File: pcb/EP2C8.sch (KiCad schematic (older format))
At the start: 1 part, among them U4 EP2C8Q208

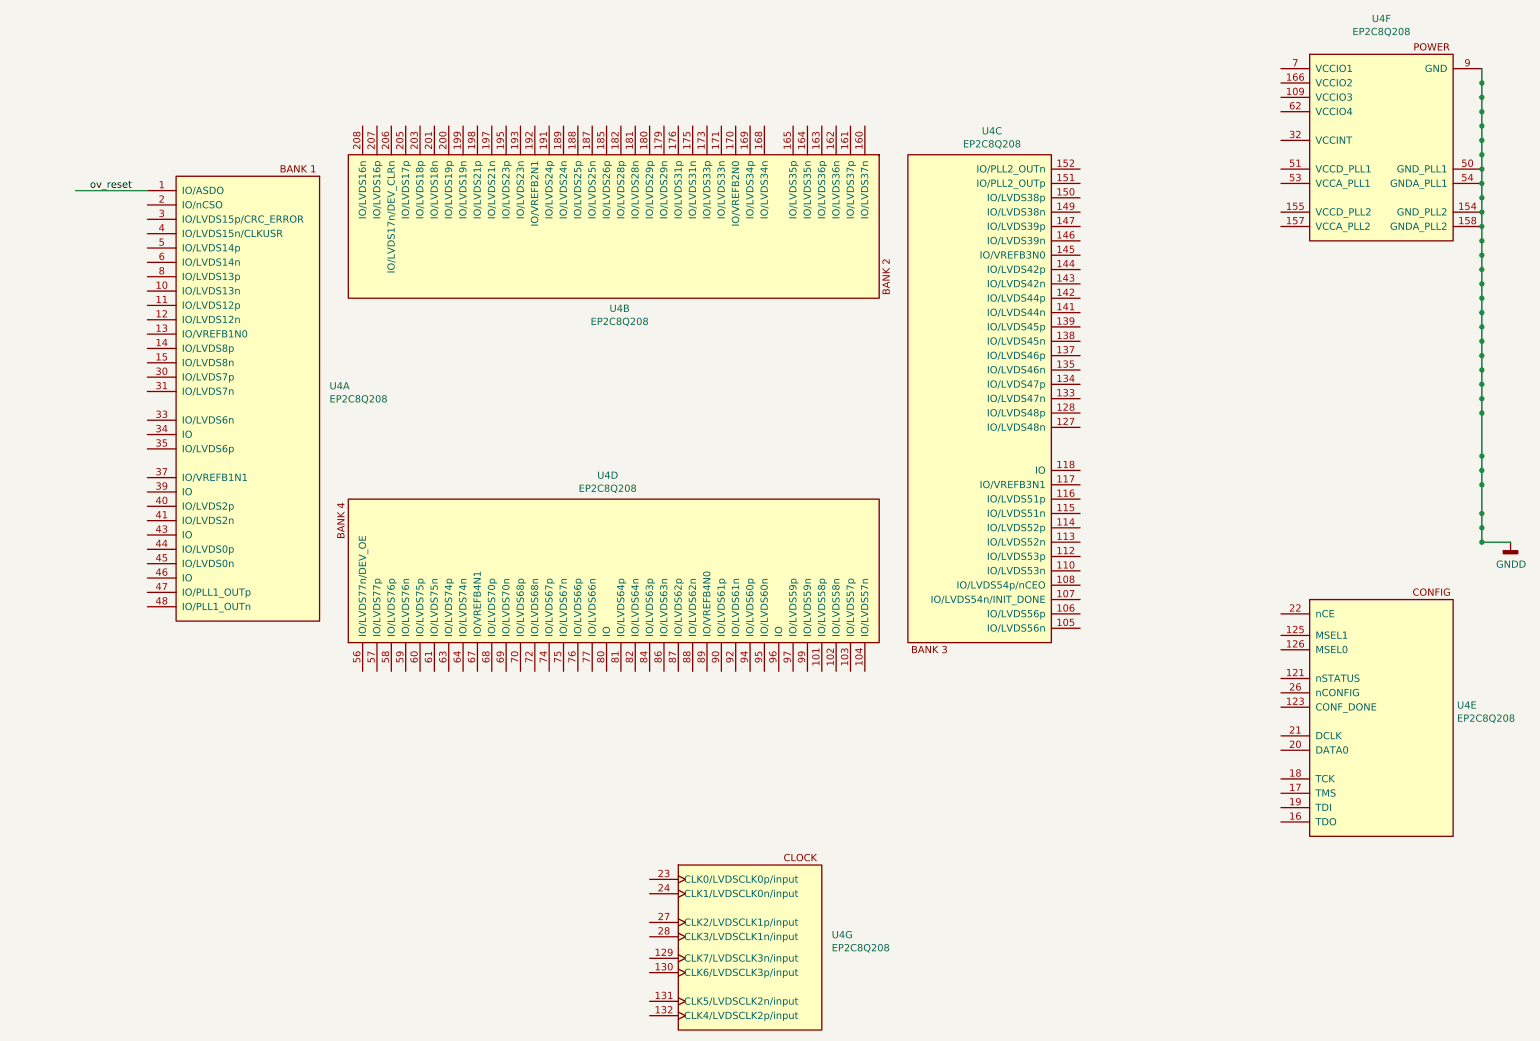
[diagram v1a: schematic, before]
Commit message: Update for latest EP2C8 symbol change.
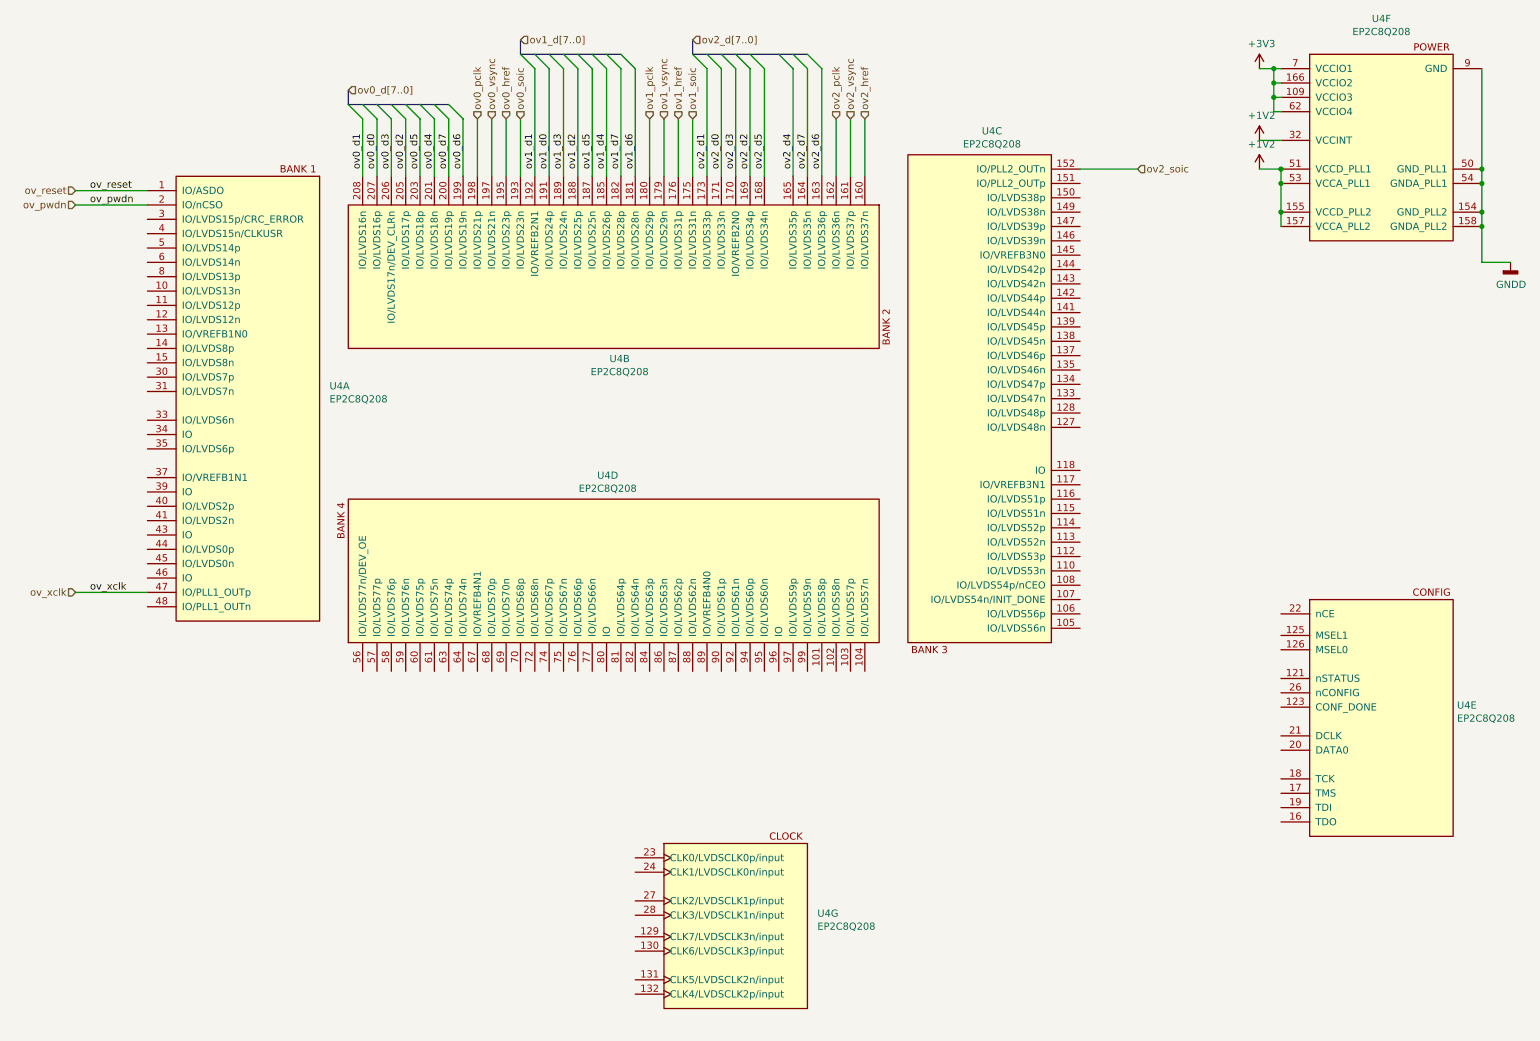
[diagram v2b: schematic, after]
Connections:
- net labels added: +1V2, +3V3, ov0_d0, ov0_d1, ov0_d2, ov0_d3, ov0_d4, ov0_d5, ov0_d6, ov0_d7, ov0_d[7..0], ov0_href, ov0_pclk, ov0_soic, ov0_vsync, ov1_d0, ov1_d1, ov1_d2, ov1_d3, ov1_d4, ov1_d5, ov1_d6, ov1_d7, ov1_d[7..0], ov1_href, ov1_pclk, ov1_soic, ov1_vsync, ov2_d0, ov2_d1, ov2_d2, ov2_d3, ov2_d4, ov2_d5, ov2_d6, ov2_d7, ov2_d[7..0], ov2_href, ov2_pclk, ov2_soic, ov2_vsync, ov_pwdn, ov_xclk
- wire segments 32 -> 58
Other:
- moved on the sheet: U4B, U4G
